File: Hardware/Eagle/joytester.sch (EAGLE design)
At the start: 12 parts

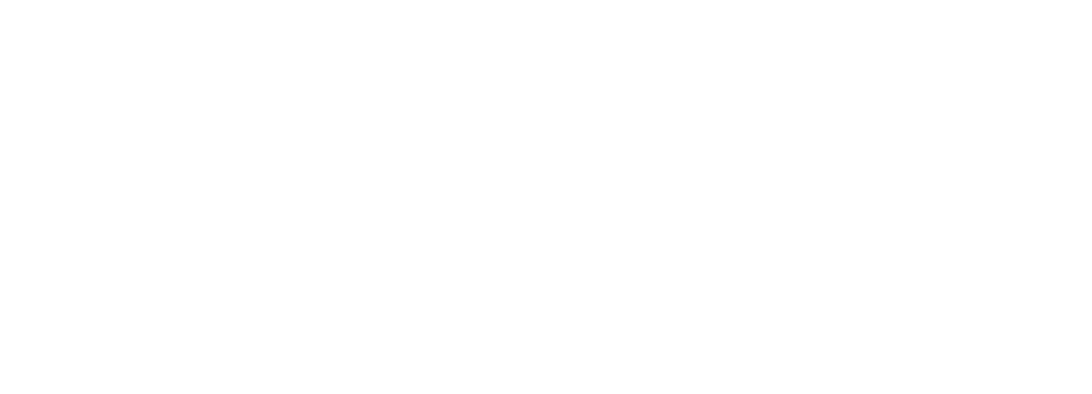
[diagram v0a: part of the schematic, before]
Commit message: Update Hardware/Eagle/joytester.sch
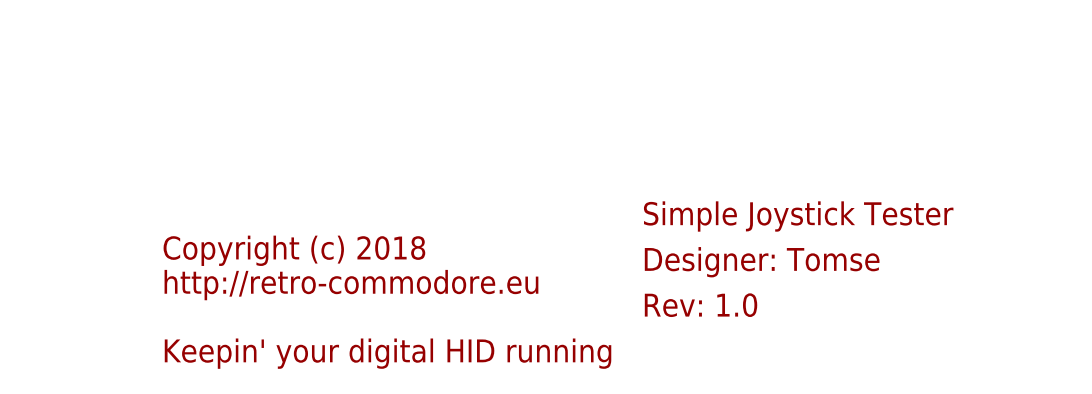
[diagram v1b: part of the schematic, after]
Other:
- note added: "Copyright (c) 2018 http://retro-commodore.eu Keepin' your digital HID running"
- note added: "Designer: Tomse"
- note added: "Rev: 1.0"
- note added: "Simple Joystick Tester"
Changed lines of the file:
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@@
 <?xml version="1.0" encoding="utf-8"?>
 <!DOCTYPE eagle SYSTEM "eagle.dtd">
-<eagle version="9.0.0">
+<eagle version="9.0.1">
 <drawing>
 <settings>
@@
 <part name="R1" library="adafruit" library_urn="urn:adsk.eagle:library:420" deviceset="R-US_" device="0207/12" value="47"/>
 <part name="R3" library="adafruit" library_urn="urn:adsk.eagle:library:420" deviceset="R-US_" device="0207/12" value="47"/>
+<part name="FRAME1" library="frames" library_urn="urn:adsk.eagle:library:229" deviceset="A4L-LOC" device=""/>
 </parts>
 <sheets>
 <sheet>
 <plain>
+<text x="81.28" y="-38.1" size="2.54" layer="94">Copyright (c) 2018
+http://retro-commodore.eu
+Keepin' your digital HID running
+</text>
+<text x="134.62" y="-22.86" size="2.54" layer="94">Simple Joystick Tester</text>
+<text x="134.62" y="-27.94" size="2.54" layer="94">Designer: Tomse</text>
+<text x="134.62" y="-33.02" size="2.54" layer="94">Rev: 1.0</text>
 </plain>
 <instances>
@@
 <instance part="R1" gate="G$1" x="20.32" y="38.1" rot="R90"/>
 <instance part="R3" gate="G$1" x="27.94" y="38.1" rot="R90"/>
+<instance part="FRAME1" gate="G$1" x="-81.28" y="-43.18" smashed="yes">
+<attribute name="SHEET" x="149.225" y="-38.1" size="2.54" layer="94"/>
+</instance>
 </instances>
 <busses>
@@
 </drawing>
 <compatibility>
+<note version="6.3" minversion="6.2.2" severity="warning">
+Since Version 6.2.2 text objects can contain more than one line,
+which will not be processed correctly with this version.
+</note>
 <note version="8.2" severity="warning">
 Since Version 8.2, EAGLE supports online libraries. The ids
